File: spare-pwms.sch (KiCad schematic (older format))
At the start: 14 parts

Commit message: Start rerouting again
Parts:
- gave numbers to parts that had none: 14
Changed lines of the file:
@@
 AR Path="/5EF79CE0/61A4756B" Ref="U?"  Part="1"
 AR Path="/5EF927DD/61A4756B" Ref="U?"  Part="1"
-AR Path="/61A19522/61A4756B" Ref="U?"  Part="1"
-F 0 "U?" H 4600 2367 50  0000 C CNN
+AR Path="/61A19522/61A4756B" Ref="U3"  Part="1"
+F 0 "U3" H 4600 2367 50  0000 C CNN
 F 1 "VNLD5090" H 4600 2276 50  0000 C CNN
 F 2 "Package_SO:SOIC-8_3.9x4.9mm_P1.27mm" H 4700 1100 50  0001 C CNN
@@
 AR Path="/5EF79CE0/61A47571" Ref="#PWR?"  Part="1"
 AR Path="/5EF927DD/61A47571" Ref="#PWR?"  Part="1"
-AR Path="/61A19522/61A47571" Ref="#PWR?"  Part="1"
-F 0 "#PWR?" H 3750 1050 50  0001 C CNN
+AR Path="/61A19522/61A47571" Ref="#PWR084"  Part="1"
+F 0 "#PWR084" H 3750 1050 50  0001 C CNN
 F 1 "GND" H 3755 1127 50  0000 C CNN
 F 2 "" H 3750 1300 50  0001 C CNN
@@
 AR Path="/5EF79CE0/61A47577" Ref="#PWR?"  Part="1"
 AR Path="/5EF927DD/61A47577" Ref="#PWR?"  Part="1"
-AR Path="/61A19522/61A47577" Ref="#PWR?"  Part="1"
-F 0 "#PWR?" H 3750 1950 50  0001 C CNN
+AR Path="/61A19522/61A47577" Ref="#PWR085"  Part="1"
+F 0 "#PWR085" H 3750 1950 50  0001 C CNN
 F 1 "GND" H 3755 2027 50  0000 C CNN
 F 2 "" H 3750 2200 50  0001 C CNN
@@
 AR Path="/5EF79CE0/61A47580" Ref="#PWR?"  Part="1"
 AR Path="/5EF927DD/61A47580" Ref="#PWR?"  Part="1"
-AR Path="/61A19522/61A47580" Ref="#PWR?"  Part="1"
-F 0 "#PWR?" H 5800 1800 50  0001 C CNN
+AR Path="/61A19522/61A47580" Ref="#PWR089"  Part="1"
+F 0 "#PWR089" H 5800 1800 50  0001 C CNN
 F 1 "GND" H 5805 1877 50  0000 C CNN
 F 2 "" H 5800 2050 50  0001 C CNN
@@
 AR Path="/5EF79CE0/61A47586" Ref="#PWR?"  Part="1"
 AR Path="/5EF927DD/61A47586" Ref="#PWR?"  Part="1"
-AR Path="/61A19522/61A47586" Ref="#PWR?"  Part="1"
-F 0 "#PWR?" H 5800 1500 50  0001 C CNN
+AR Path="/61A19522/61A47586" Ref="#PWR088"  Part="1"
+F 0 "#PWR088" H 5800 1500 50  0001 C CNN
 F 1 "GND" H 5805 1577 50  0000 C CNN
 F 2 "" H 5800 1750 50  0001 C CNN
@@
 AR Path="/5EEDB4C5/61A47594" Ref="R?"  Part="1"
 AR Path="/5EF927DD/61A47594" Ref="R?"  Part="1"
-AR Path="/61A19522/61A47594" Ref="R?"  Part="1"
-F 0 "R?" V 2993 1600 50  0000 C CNN
+AR Path="/61A19522/61A47594" Ref="R81"  Part="1"
+F 0 "R81" V 2993 1600 50  0000 C CNN
 F 1 "1k" V 3084 1600 50  0000 C CNN
 F 2 "Resistor_SMD:R_0603_1608Metric_Pad0.98x0.95mm_HandSolder" V 3130 1600 50  0001 C CNN
@@
 AR Path="/5EEDB4C5/61A4759D" Ref="R?"  Part="1"
 AR Path="/5EF927DD/61A4759D" Ref="R?"  Part="1"
-AR Path="/61A19522/61A4759D" Ref="R?"  Part="1"
-F 0 "R?" V 2993 1900 50  0000 C CNN
+AR Path="/61A19522/61A4759D" Ref="R82"  Part="1"
+F 0 "R82" V 2993 1900 50  0000 C CNN
 F 1 "1k" V 3084 1900 50  0000 C CNN
 F 2 "Resistor_SMD:R_0603_1608Metric_Pad0.98x0.95mm_HandSolder" V 3130 1900 50  0001 C CNN
@@
 AR Path="/5EEDB4C5/61A475A8" Ref="R?"  Part="1"
 AR Path="/5EF927DD/61A475A8" Ref="R?"  Part="1"
-AR Path="/61A19522/61A475A8" Ref="R?"  Part="1"
-F 0 "R?" H 3680 2004 50  0000 R CNN
+AR Path="/61A19522/61A475A8" Ref="R86"  Part="1"
+F 0 "R86" H 3680 2004 50  0000 R CNN
 F 1 "100k" H 3680 2095 50  0000 R CNN
 F 2 "Resistor_SMD:R_0603_1608Metric_Pad0.98x0.95mm_HandSolder" V 3680 2050 50  0001 C CNN
@@
 AR Path="/5EEDB4C5/61A475B3" Ref="R?"  Part="1"
 AR Path="/5EF927DD/61A475B3" Ref="R?"  Part="1"
-AR Path="/61A19522/61A475B3" Ref="R?"  Part="1"
-F 0 "R?" H 3680 1404 50  0000 R CNN
+AR Path="/61A19522/61A475B3" Ref="R85"  Part="1"
+F 0 "R85" H 3680 1404 50  0000 R CNN
 F 1 "100k" H 3680 1495 50  0000 R CNN
 F 2 "Resistor_SMD:R_0603_1608Metric_Pad0.98x0.95mm_HandSolder" V 3680 1450 50  0001 C CNN
@@
 AR Path="/5EF79CE0/61A475BE" Ref="D?"  Part="1"
 AR Path="/5EF927DD/61A475BE" Ref="D?"  Part="1"
-AR Path="/61A19522/61A475BE" Ref="D?"  Part="1"
-F 0 "D?" V 6200 2250 50  0000 L CNN
+AR Path="/61A19522/61A475BE" Ref="D31"  Part="1"
+F 0 "D31" V 6200 2250 50  0000 L CNN
 F 1 "1n41001" V 6100 2000 50  0000 L CNN
 F 2 "Diode_SMD:D_SOD-123" H 6150 2450 50  0001 C CNN
@@
 AR Path="/5EF79CE0/61A475CC" Ref="D?"  Part="1"
 AR Path="/5EF927DD/61A475CC" Ref="D?"  Part="1"
-AR Path="/61A19522/61A475CC" Ref="D?"  Part="1"
-F 0 "D?" V 6104 1480 50  0000 L CNN
+AR Path="/61A19522/61A475CC" Ref="D21"  Part="1"
+F 0 "D21" V 6104 1480 50  0000 L CNN
 F 1 "1n41001" V 6195 1480 50  0000 L CNN
 F 2 "Diode_SMD:D_SOD-123" H 6150 1400 50  0001 C CNN
@@
 AR Path="/5EF79CE0/61A4947D" Ref="U?"  Part="1"
 AR Path="/5EF927DD/61A4947D" Ref="U?"  Part="1"
-AR Path="/61A19522/61A4947D" Ref="U?"  Part="1"
-F 0 "U?" H 4600 5017 50  0000 C CNN
+AR Path="/61A19522/61A4947D" Ref="U7"  Part="1"
+F 0 "U7" H 4600 5017 50  0000 C CNN
 F 1 "VNLD5090" H 4600 4926 50  0000 C CNN
 F 2 "Package_SO:SOIC-8_3.9x4.9mm_P1.27mm" H 4700 3750 50  0001 C CNN
@@
 AR Path="/5EF79CE0/61A49483" Ref="#PWR?"  Part="1"
 AR Path="/5EF927DD/61A49483" Ref="#PWR?"  Part="1"
-AR Path="/61A19522/61A49483" Ref="#PWR?"  Part="1"
-F 0 "#PWR?" H 3750 3700 50  0001 C CNN
+AR Path="/61A19522/61A49483" Ref="#PWR086"  Part="1"
+F 0 "#PWR086" H 3750 3700 50  0001 C CNN
 F 1 "GND" H 3755 3777 50  0000 C CNN
 F 2 "" H 3750 3950 50  0001 C CNN
@@
 AR Path="/5EF79CE0/61A49489" Ref="#PWR?"  Part="1"
 AR Path="/5EF927DD/61A49489" Ref="#PWR?"  Part="1"
-AR Path="/61A19522/61A49489" Ref="#PWR?"  Part="1"
-F 0 "#PWR?" H 3750 4600 50  0001 C CNN
+AR Path="/61A19522/61A49489" Ref="#PWR087"  Part="1"
+F 0 "#PWR087" H 3750 4600 50  0001 C CNN
 F 1 "GND" H 3755 4677 50  0000 C CNN
 F 2 "" H 3750 4850 50  0001 C CNN
@@
 AR Path="/5EF79CE0/61A49492" Ref="#PWR?"  Part="1"
 AR Path="/5EF927DD/61A49492" Ref="#PWR?"  Part="1"
-AR Path="/61A19522/61A49492" Ref="#PWR?"  Part="1"
-F 0 "#PWR?" H 5800 4450 50  0001 C CNN
+AR Path="/61A19522/61A49492" Ref="#PWR091"  Part="1"
+F 0 "#PWR091" H 5800 4450 50  0001 C CNN
 F 1 "GND" H 5805 4527 50  0000 C CNN
 F 2 "" H 5800 4700 50  0001 C CNN
@@
 AR Path="/5EF79CE0/61A49498" Ref="#PWR?"  Part="1"
 AR Path="/5EF927DD/61A49498" Ref="#PWR?"  Part="1"
-AR Path="/61A19522/61A49498" Ref="#PWR?"  Part="1"
-F 0 "#PWR?" H 5800 4150 50  0001 C CNN
+AR Path="/61A19522/61A49498" Ref="#PWR090"  Part="1"
+F 0 "#PWR090" H 5800 4150 50  0001 C CNN
 F 1 "GND" H 5805 4227 50  0000 C CNN
 F 2 "" H 5800 4400 50  0001 C CNN
@@
 AR Path="/5EEDB4C5/61A494A6" Ref="R?"  Part="1"
 AR Path="/5EF927DD/61A494A6" Ref="R?"  Part="1"
-AR Path="/61A19522/61A494A6" Ref="R?"  Part="1"
-F 0 "R?" V 2993 4250 50  0000 C CNN
+AR Path="/61A19522/61A494A6" Ref="R83"  Part="1"
+F 0 "R83" V 2993 4250 50  0000 C CNN
 F 1 "1k" V 3084 4250 50  0000 C CNN
 F 2 "Resistor_SMD:R_0603_1608Metric_Pad0.98x0.95mm_HandSolder" V 3130 4250 50  0001 C CNN
@@
 AR Path="/5EEDB4C5/61A494AF" Ref="R?"  Part="1"
 AR Path="/5EF927DD/61A494AF" Ref="R?"  Part="1"
-AR Path="/61A19522/61A494AF" Ref="R?"  Part="1"
-F 0 "R?" V 2993 4550 50  0000 C CNN
+AR Path="/61A19522/61A494AF" Ref="R84"  Part="1"
+F 0 "R84" V 2993 4550 50  0000 C CNN
 F 1 "1k" V 3084 4550 50  0000 C CNN
 F 2 "Resistor_SMD:R_0603_1608Metric_Pad0.98x0.95mm_HandSolder" V 3130 4550 50  0001 C CNN
@@
 AR Path="/5EEDB4C5/61A494BA" Ref="R?"  Part="1"
 AR Path="/5EF927DD/61A494BA" Ref="R?"  Part="1"
-AR Path="/61A19522/61A494BA" Ref="R?"  Part="1"
-F 0 "R?" H 3680 4654 50  0000 R CNN
+AR Path="/61A19522/61A494BA" Ref="R88"  Part="1"
+F 0 "R88" H 3680 4654 50  0000 R CNN
 F 1 "100k" H 3680 4745 50  0000 R CNN
 F 2 "Resistor_SMD:R_0603_1608Metric_Pad0.98x0.95mm_HandSolder" V 3680 4700 50  0001 C CNN
@@
 AR Path="/5EEDB4C5/61A494C5" Ref="R?"  Part="1"
 AR Path="/5EF927DD/61A494C5" Ref="R?"  Part="1"
-AR Path="/61A19522/61A494C5" Ref="R?"  Part="1"
-F 0 "R?" H 3680 4054 50  0000 R CNN
+AR Path="/61A19522/61A494C5" Ref="R87"  Part="1"
+F 0 "R87" H 3680 4054 50  0000 R CNN
 F 1 "100k" H 3680 4145 50  0000 R CNN
 F 2 "Resistor_SMD:R_0603_1608Metric_Pad0.98x0.95mm_HandSolder" V 3680 4100 50  0001 C CNN
@@
 AR Path="/5EF79CE0/61A494D0" Ref="D?"  Part="1"
 AR Path="/5EF927DD/61A494D0" Ref="D?"  Part="1"
-AR Path="/61A19522/61A494D0" Ref="D?"  Part="1"
-F 0 "D?" V 6200 4900 50  0000 L CNN
+AR Path="/61A19522/61A494D0" Ref="D33"  Part="1"
+F 0 "D33" V 6200 4900 50  0000 L CNN
 F 1 "1n41001" V 6100 4650 50  0000 L CNN
 F 2 "Diode_SMD:D_SOD-123" H 6150 5100 50  0001 C CNN
@@
 AR Path="/5EF79CE0/61A494DE" Ref="D?"  Part="1"
 AR Path="/5EF927DD/61A494DE" Ref="D?"  Part="1"
-AR Path="/61A19522/61A494DE" Ref="D?"  Part="1"
-F 0 "D?" V 6104 4130 50  0000 L CNN
+AR Path="/61A19522/61A494DE" Ref="D32"  Part="1"
+F 0 "D32" V 6104 4130 50  0000 L CNN
 F 1 "1n41001" V 6195 4130 50  0000 L CNN
 F 2 "Diode_SMD:D_SOD-123" H 6150 4050 50  0001 C CNN

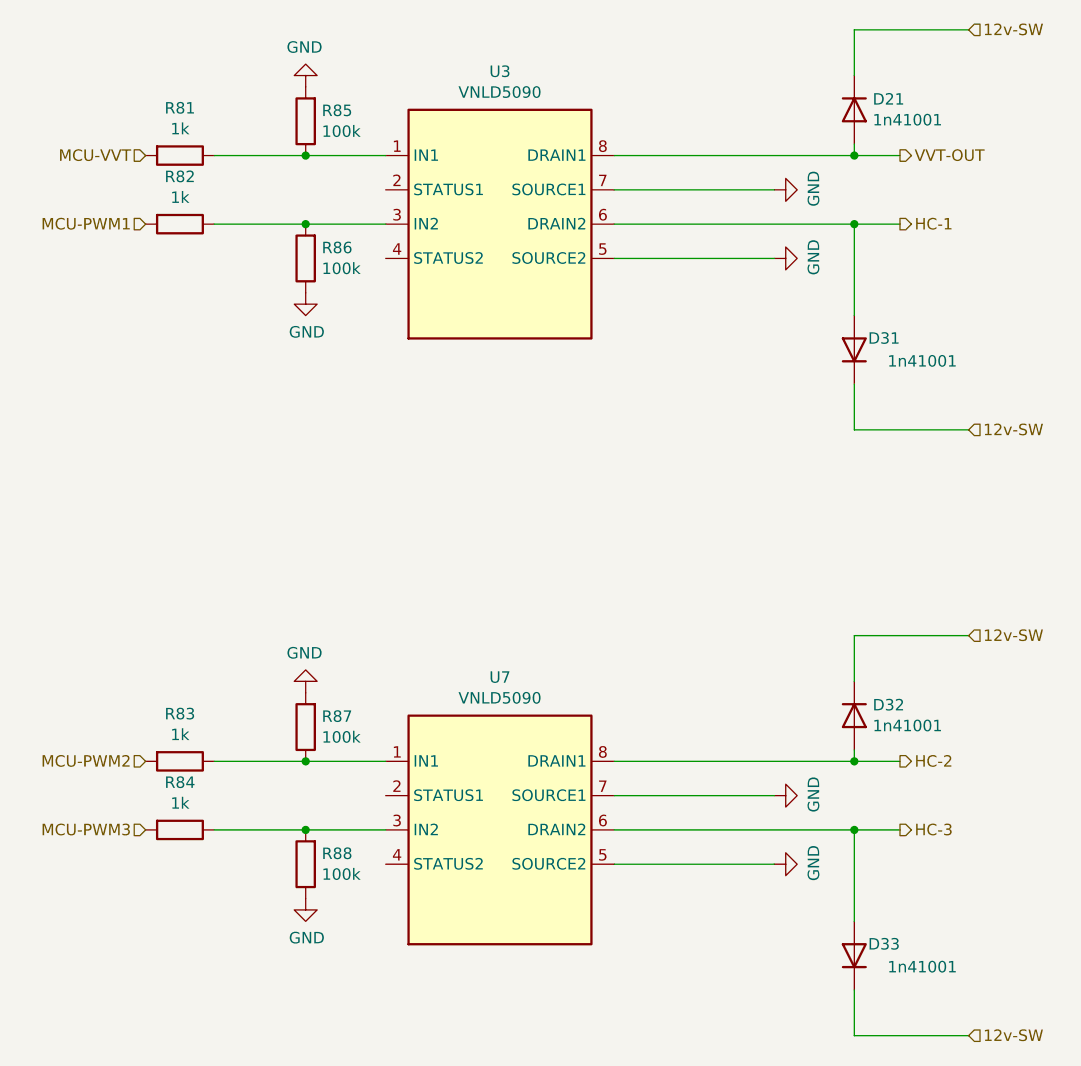
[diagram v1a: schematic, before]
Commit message: Schematic and Layout Updates
* cleanup unused pins for DRC
* swap swd connector for the fancy one the phill uses
* swap out the CAN transciever for one more suitable for 3v3
* reroute CAN differential pair
* clean up copper pours
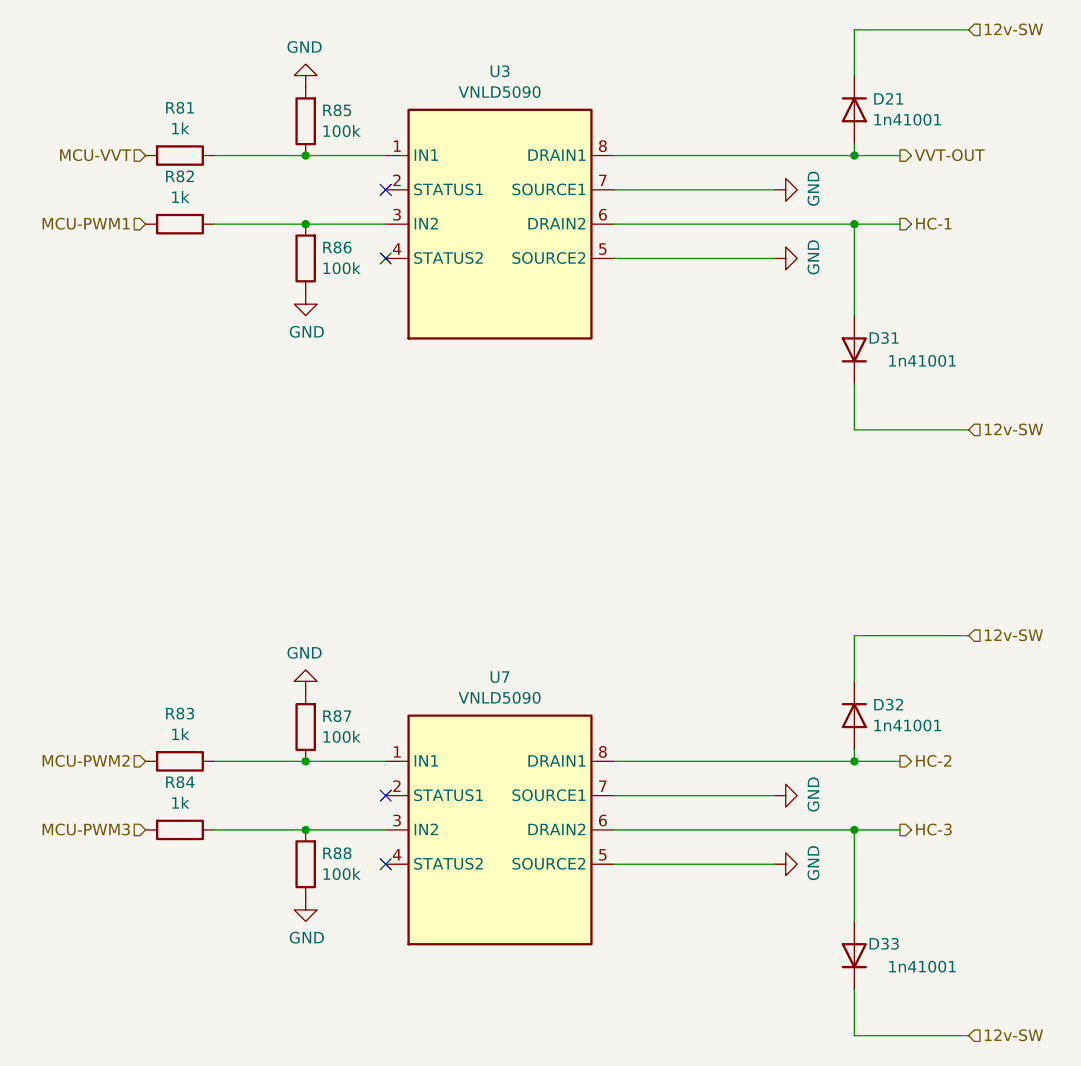
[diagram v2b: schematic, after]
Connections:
- no-connect marks 0 -> 4
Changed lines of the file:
@@
 Text HLabel 3050 1900 0    50   Input ~ 0
 MCU-PWM1
+NoConn ~ 4100 4400
+NoConn ~ 4100 4700
+NoConn ~ 4100 1750
+NoConn ~ 4100 2050
 $EndSCHEMATC
